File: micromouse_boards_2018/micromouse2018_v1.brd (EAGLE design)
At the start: 86 x 65 mm, 55 parts, among them IC1 TPS562210DDFT

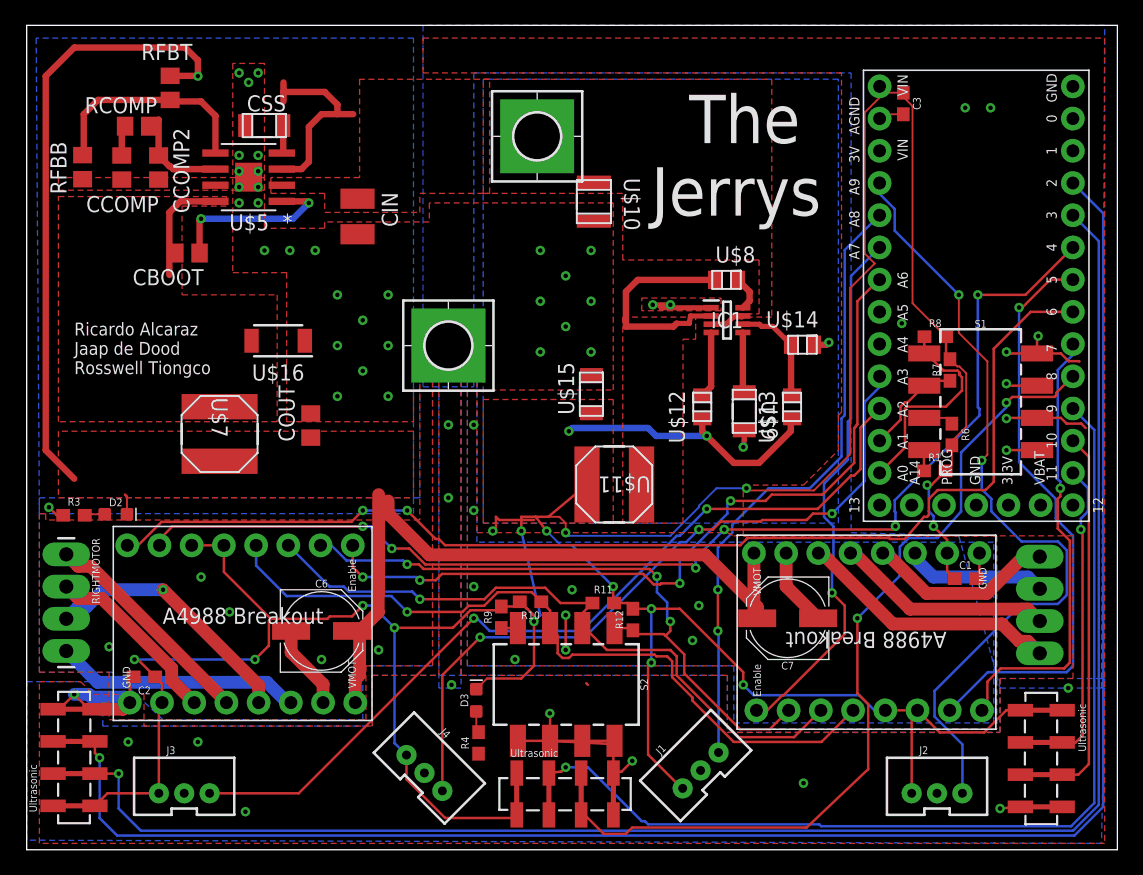
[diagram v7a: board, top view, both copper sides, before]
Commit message: Made mounting holes a bit smaller
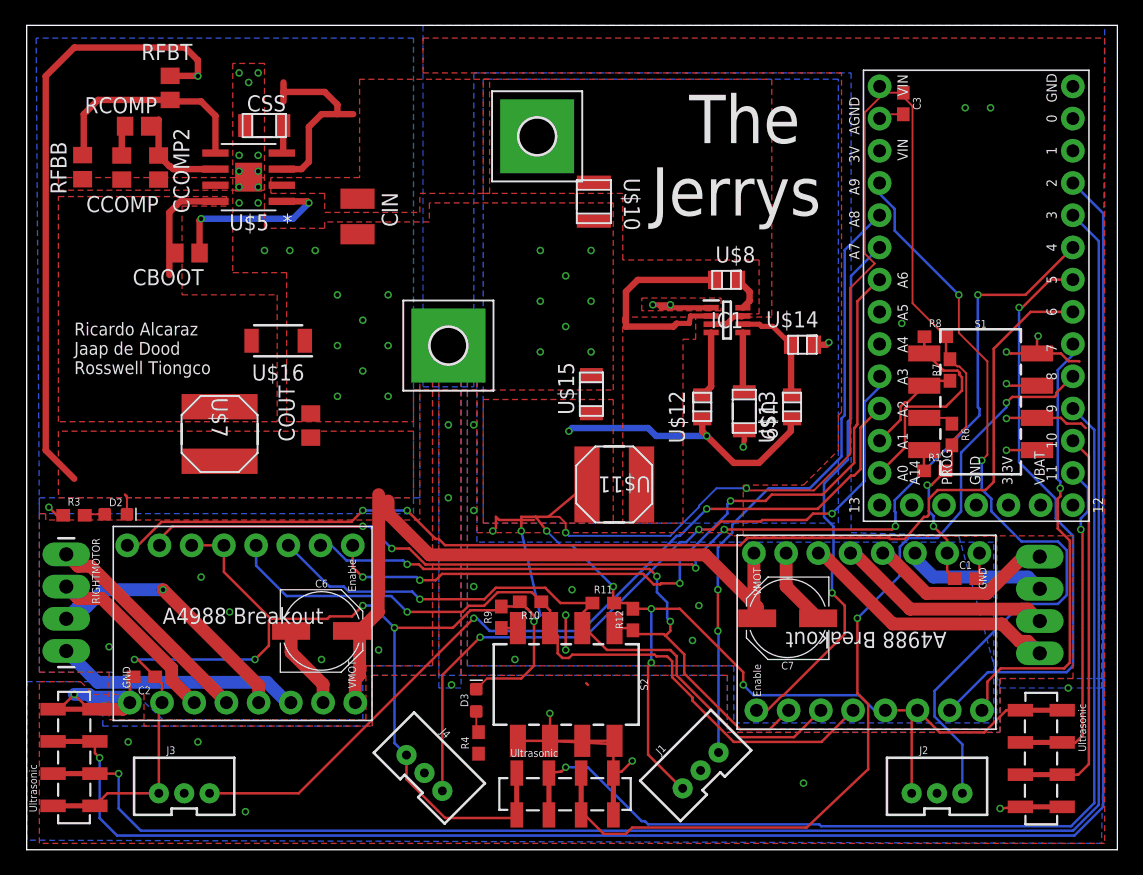
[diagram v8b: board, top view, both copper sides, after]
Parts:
- H1, H2: value MOUNT-PAD-SQUARE3.6 -> MOUNT-PAD-SQUARE2.8; device holes:3,6-PAD-SQUARE -> holes:2,8-PAD-SQUARE
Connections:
- net GND: now also H2.B2,8; no longer H2.B3,6
- net VIN: now also H1.B2,8; no longer H1.B3,6
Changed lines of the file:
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@@
 <?xml version="1.0" encoding="utf-8"?>
 <!DOCTYPE eagle SYSTEM "eagle.dtd">
-<eagle version="8.3.2">
+<eagle version="8.7.1">
 <drawing>
 <settings>
@@
 <setting verticaltext="up"/>
 </settings>
-<grid distance="0.25" unitdist="mm" unit="mm" style="lines" multiple="1" display="yes" altdistance="0.125" altunitdist="mm" altunit="mm"/>
+<grid distance="1" unitdist="mm" unit="mm" style="lines" multiple="1" display="yes" altdistance="0.125" altunitdist="mm" altunit="mm"/>
 <layers>
 <layer number="1" name="Top" color="4" fill="1" visible="yes" active="yes"/>
+<layer number="2" name="Route2" color="1" fill="3" visible="no" active="no"/>
+<layer number="3" name="Route3" color="4" fill="3" visible="no" active="no"/>
+<layer number="4" name="Route4" color="1" fill="4" visible="no" active="no"/>
+<layer number="5" name="Route5" color="4" fill="4" visible="no" active="no"/>
+<layer number="6" name="Route6" color="1" fill="8" visible="no" active="no"/>
+<layer number="7" name="Route7" color="4" fill="8" visible="no" active="no"/>
+<layer number="8" name="Route8" color="1" fill="2" visible="no" active="no"/>
+<layer number="9" name="Route9" color="4" fill="2" visible="no" active="no"/>
+<layer number="10" name="Route10" color="1" fill="7" visible="no" active="no"/>
+<layer number="11" name="Route11" color="4" fill="7" visible="no" active="no"/>
+<layer number="12" name="Route12" color="1" fill="5" visible="no" active="no"/>
+<layer number="13" name="Route13" color="4" fill="5" visible="no" active="no"/>
+<layer number="14" name="Route14" color="1" fill="6" visible="no" active="no"/>
+<layer number="15" name="Route15" color="4" fill="6" visible="no" active="no"/>
 <layer number="16" name="Bottom" color="1" fill="1" visible="yes" active="yes"/>
 <layer number="17" name="Pads" color="2" fill="1" visible="yes" active="yes"/>
@@
 <layer number="25" name="tNames" color="7" fill="1" visible="yes" active="yes"/>
 <layer number="26" name="bNames" color="7" fill="1" visible="yes" active="yes"/>
-<layer number="27" name="tValues" color="7" fill="1" visible="no" active="yes"/>
-<layer number="28" name="bValues" color="7" fill="1" visible="no" active="yes"/>
+<layer number="27" name="tValues" color="7" fill="1" visible="yes" active="yes"/>
+<layer number="28" name="bValues" color="7" fill="1" visible="yes" active="yes"/>
 <layer number="29" name="tStop" color="7" fill="3" visible="no" active="yes"/>
 <layer number="30" name="bStop" color="7" fill="6" visible="no" active="yes"/>
@@
 <layer number="59" name="tCarbon" color="7" fill="1" visible="no" active="no"/>
 <layer number="60" name="bCarbon" color="7" fill="1" visible="no" active="no"/>
-<layer number="88" name="SimResults" color="9" fill="1" visible="no" active="yes"/>
-<layer number="89" name="SimProbes" color="9" fill="1" visible="no" active="yes"/>
+<layer number="88" name="SimResults" color="9" fill="1" visible="no" active="no"/>
+<layer number="89" name="SimProbes" color="9" fill="1" visible="no" active="no"/>
 <layer number="90" name="Modules" color="5" fill="1" visible="no" active="no"/>
 <layer number="91" name="Nets" color="2" fill="1" visible="no" active="no"/>
@@
 </class>
 </classes>
-<designrules name="default">
-<description language="de">&lt;b&gt;EAGLE Design Rules&lt;/b&gt;
+<designrules name="oshpark-2layer">
+<description language="en">&lt;b&gt;OSH Park Design Rules&lt;/b&gt;
 &lt;p&gt;
-Die Standard-Design-Rules sind so gewählt, dass sie für
-die meisten Anwendungen passen. Sollte ihre Platine
-besondere Anforderungen haben, treffen Sie die erforderlichen
-Einstellungen hier und speichern die Design Rules unter
-einem neuen Namen ab.</description>
-<description language="en">&lt;b&gt;EAGLE Design Rules&lt;/b&gt;
+Please make sure your boards conform to these design rules.
+&lt;/p&gt;
 &lt;p&gt;
-The default Design Rules have been set to cover
-a wide range of applications. Your particular design
-may have different requirements, so please make the
-necessary adjustments and save your customized
-design rules under a new name.</description>
+Note, that not all DRC settings must be set by the manufacturer. Several can be adjusted for the design, including those listed on our docs page here.
+&lt;a href=&quot;http://docs.oshpark.com/design-tools/eagle/design-rules-files/&quot;&gt;Adjustable Settings&lt;/a&gt;
+&lt;/p&gt;</description>
 <param name="layerSetup" value="(1*16)"/>
-<param name="mtCopper" value="0.035mm 0.035mm 0.035mm 0.035mm 0.035mm 0.035mm 0.035mm 0.035mm 0.035mm 0.035mm 0.035mm 0.035mm 0.035mm 0.035mm 0.035mm 0.035mm"/>
-<param name="mtIsolate" value="1.5mm 0.15mm 0.2mm 0.15mm 0.2mm 0.15mm 0.2mm 0.15mm 0.2mm 0.15mm 0.2mm 0.15mm 0.2mm 0.15mm 0.2mm"/>
+<param name="mtCopper" value="0.035559375mm 0.0356mm 0.0356mm 0.0356mm 0.0356mm 0.0356mm 0.0356mm 0.0356mm 0.0356mm 0.0356mm 0.0356mm 0.0356mm 0.0356mm 0.0356mm 0.0356mm 0.035559375mm"/>
+<param name="mtIsolate" value="1.6mm 0.1499mm 0.2007mm 0.1499mm 0.2007mm 0.1499mm 0.2007mm 0.1499mm 0.2007mm 0.1499mm 0.2007mm 0.1499mm 0.2007mm 0.1499mm 0.2007mm"/>
 <param name="mdWireWire" value="6mil"/>
 <param name="mdWirePad" value="6mil"/>
@@
 <param name="mdSmdVia" value="6mil"/>
 <param name="mdSmdSmd" value="6mil"/>
-<param name="mdViaViaSameLayer" value="6mil"/>
+<param name="mdViaViaSameLayer" value="8mil"/>
 <param name="mnLayersViaInSmd" value="2"/>
-<param name="mdCopperDimension" value="40mil"/>
+<param name="mdCopperDimension" value="15mil"/>
 <param name="mdDrill" value="6mil"/>
 <param name="mdSmdStop" value="0mil"/>
 <param name="msWidth" value="6mil"/>
-<param name="msDrill" value="0.35mm"/>
-<param name="msMicroVia" value="9.99mm"/>
+<param name="msDrill" value="10mil"/>
+<param name="msMicroVia" value="10mil"/>
 <param name="msBlindViaRatio" value="0.5"/>
 <param name="rvPadTop" value="0.25"/>
@@
 <param name="rvMicroViaOuter" value="0.25"/>
 <param name="rvMicroViaInner" value="0.25"/>
-<param name="rlMinPadTop" value="10mil"/>
+<param name="rlMinPadTop" value="5mil"/>
 <param name="rlMaxPadTop" value="20mil"/>
-<param name="rlMinPadInner" value="10mil"/>
+<param name="rlMinPadInner" value="5mil"/>
 <param name="rlMaxPadInner" value="20mil"/>
-<param name="rlMinPadBottom" value="10mil"/>
+<param name="rlMinPadBottom" value="5mil"/>
 <param name="rlMaxPadBottom" value="20mil"/>
-<param name="rlMinViaOuter" value="8mil"/>
+<param name="rlMinViaOuter" value="5mil"/>
 <param name="rlMaxViaOuter" value="20mil"/>
-<param name="rlMinViaInner" value="8mil"/>
+<param name="rlMinViaInner" value="5mil"/>
 <param name="rlMaxViaInner" value="20mil"/>
-<param name="rlMinMicroViaOuter" value="4mil"/>
+<param name="rlMinMicroViaOuter" value="5mil"/>
 <param name="rlMaxMicroViaOuter" value="20mil"/>
-<param name="rlMinMicroViaInner" value="4mil"/>
+<param name="rlMinMicroViaInner" value="5mil"/>
 <param name="rlMaxMicroViaInner" value="20mil"/>
 <param name="psTop" value="-1"/>
@@
 <param name="mvStopFrame" value="1"/>
 <param name="mvCreamFrame" value="0"/>
-<param name="mlMinStopFrame" value="4mil"/>
-<param name="mlMaxStopFrame" value="4mil"/>
+<param name="mlMinStopFrame" value="2.5mil"/>
+<param name="mlMaxStopFrame" value="2.5mil"/>
 <param name="mlMinCreamFrame" value="0mil"/>
 <param name="mlMaxCreamFrame" value="0mil"/>
@@
 <param name="dpMaxLengthDifference" value="10mm"/>
 <param name="dpGapFactor" value="2.5"/>
-<param name="checkGrid" value="0"/>
 <param name="checkAngle" value="0"/>
 <param name="checkFont" value="1"/>
 <param name="checkRestrict" value="1"/>
+<param name="checkStop" value="0"/>
+<param name="checkValues" value="0"/>
 <param name="useDiameter" value="13"/>
 <param name="maxErrors" value="50"/>
@@
 <attribute name="VALUE" x="19.83" y="42.38" size="1.27" layer="27" rot="R180" align="center"/>
 </element>
-<element name="H1" library="holes" library_urn="urn:adsk.eagle:library:237" package="3,6-PAD-SQUARE" package3d_urn="urn:adsk.eagle:package:14294/1" value="MOUNT-PAD-SQUARE3.6" x="40.25" y="56.25"/>
-<element name="H2" library="holes" library_urn="urn:adsk.eagle:library:237" package="3,6-PAD-SQUARE" package3d_urn="urn:adsk.eagle:package:14294/1" value="MOUNT-PAD-SQUARE3.6" x="33.25" y="39.75"/>
+<element name="H1" library="holes" library_urn="urn:adsk.eagle:library:237" package="2,8-PAD-SQUARE" package3d_urn="urn:adsk.eagle:package:14300/1" value="MOUNT-PAD-SQUARE2.8" x="40.25" y="56.25"/>
+<element name="H2" library="holes" library_urn="urn:adsk.eagle:library:237" package="2,8-PAD-SQUARE" package3d_urn="urn:adsk.eagle:package:14300/1" value="MOUNT-PAD-SQUARE2.8" x="33.25" y="39.75"/>
 <element name="U$6" library="raParts" package="1X04_SMD_VERTICAL_COMBO" value="ULTRASONIC" x="80" y="11" rot="R270"/>
 <element name="C6" library="SparkFun-Capacitors" package="PANASONIC_D" value="100uF" x="23.25" y="17.25">
@@
 <wire x1="42.5" y1="18.75" x2="42.5" y2="18.5" width="0.2" layer="1"/>
 <via x="42.5" y="18.5" extent="1-16" drill="0.35"/>
-<contactref element="H2" pad="B3,6"/>
+<contactref element="H2" pad="B2,8"/>
 </signal>
 <signal name="ENABLE1">
@@
 <vertex x="26.25" y="60.75"/>
 </polygon>
-<contactref element="H1" pad="B3,6"/>
+<contactref element="H1" pad="B2,8"/>
 </signal>
 <signal name="N$8">
